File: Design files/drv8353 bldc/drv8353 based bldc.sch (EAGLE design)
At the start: 117 parts, among them IC1 DRV8353RSRGZT, J3 2X6 FEMALE, J4 B06B-HCMKK, Q1 FDBL86062-F085, Q2 FDBL86062-F085, Q3 FDBL86062-F085, Q4 FDBL86062-F085, Q5 FDBL86062-F085, Q6 FDBL86062-F085

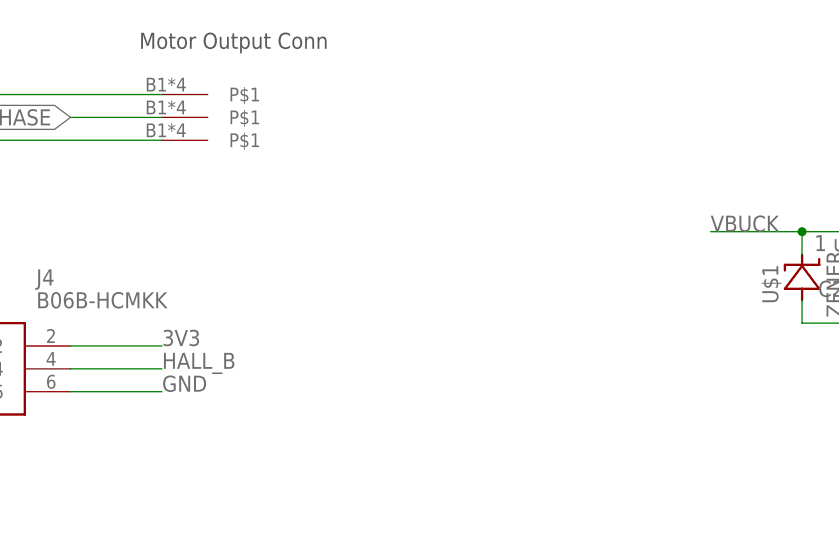
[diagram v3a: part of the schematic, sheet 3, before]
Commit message: adds correct circuitry for hall effect sensors
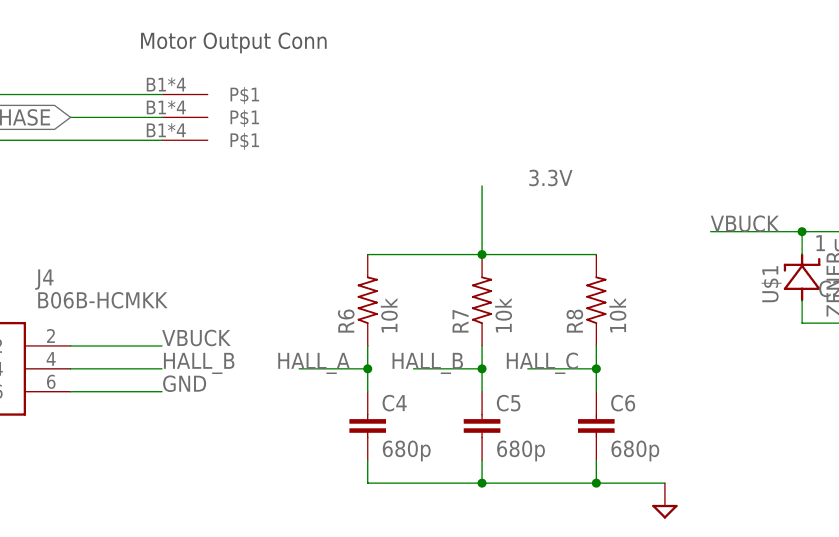
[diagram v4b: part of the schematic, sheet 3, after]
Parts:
- added C4, C5, C6: 680p, rcl:C-EUC0603K
- added R6, R7, R8: 10k, rcl:R-US_R0603
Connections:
- new net 3.3V: R6.2, R7.2, R8.2
- net 3V3: no longer J4.2
- net GND: now also C4.2, C5.2, C6.2
- net HALL_A: now also C4.1, R6.1
- net HALL_B: now also C5.1, R7.1
- net HALL_C: now also C6.1, R8.1
- net VBUCK: now also J4.2
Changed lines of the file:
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@@
 <part name="Q5" library="SamacSys_Parts" deviceset="FDBL86062-F085" device=""/>
 <part name="Q6" library="SamacSys_Parts" deviceset="FDBL86062-F085" device=""/>
+<part name="R6" library="rcl" library_urn="urn:adsk.eagle:library:334" deviceset="R-US_" device="R0603" package3d_urn="urn:adsk.eagle:package:23555/3" value="10k"/>
+<part name="R7" library="rcl" library_urn="urn:adsk.eagle:library:334" deviceset="R-US_" device="R0603" package3d_urn="urn:adsk.eagle:package:23555/3" value="10k"/>
+<part name="R8" library="rcl" library_urn="urn:adsk.eagle:library:334" deviceset="R-US_" device="R0603" package3d_urn="urn:adsk.eagle:package:23555/3" value="10k"/>
+<part name="C4" library="rcl" library_urn="urn:adsk.eagle:library:334" deviceset="C-EU" device="C0603K" package3d_urn="urn:adsk.eagle:package:23680/2" value="680p"/>
+<part name="C5" library="rcl" library_urn="urn:adsk.eagle:library:334" deviceset="C-EU" device="C0603K" package3d_urn="urn:adsk.eagle:package:23680/2" value="680p"/>
+<part name="C6" library="rcl" library_urn="urn:adsk.eagle:library:334" deviceset="C-EU" device="C0603K" package3d_urn="urn:adsk.eagle:package:23680/2" value="680p"/>
+<part name="SUPPLY12" library="supply2" library_urn="urn:adsk.eagle:library:372" deviceset="GND" device=""/>
 </parts>
 <sheets>
@@
 <attribute name="VALUE" x="201.93" y="-12.7" size="1.778" layer="96"/>
 </instance>
+<instance part="R6" gate="G$1" x="78.74" y="-10.16" smashed="yes" rot="R90">
+<attribute name="NAME" x="77.2414" y="-13.97" size="1.778" layer="95" rot="R90"/>
+<attribute name="VALUE" x="82.042" y="-13.97" size="1.778" layer="96" rot="R90"/>
+</instance>
+<instance part="R7" gate="G$1" x="91.44" y="-10.16" smashed="yes" rot="R90">
+<attribute name="NAME" x="89.9414" y="-13.97" size="1.778" layer="95" rot="R90"/>
+<attribute name="VALUE" x="94.742" y="-13.97" size="1.778" layer="96" rot="R90"/>
+</instance>
+<instance part="R8" gate="G$1" x="104.14" y="-10.16" smashed="yes" rot="R90">
+<attribute name="NAME" x="102.6414" y="-13.97" size="1.778" layer="95" rot="R90"/>
+<attribute name="VALUE" x="107.442" y="-13.97" size="1.778" layer="96" rot="R90"/>
+</instance>
+<instance part="C4" gate="G$1" x="78.74" y="-22.86" smashed="yes">
+<attribute name="NAME" x="80.264" y="-22.479" size="1.778" layer="95"/>
+<attribute name="VALUE" x="80.264" y="-27.559" size="1.778" layer="96"/>
+</instance>
+<instance part="C5" gate="G$1" x="91.44" y="-22.86" smashed="yes">
+<attribute name="NAME" x="92.964" y="-22.479" size="1.778" layer="95"/>
+<attribute name="VALUE" x="92.964" y="-27.559" size="1.778" layer="96"/>
+</instance>
+<instance part="C6" gate="G$1" x="104.14" y="-22.86" smashed="yes">
+<attribute name="NAME" x="105.664" y="-22.479" size="1.778" layer="95"/>
+<attribute name="VALUE" x="105.664" y="-27.559" size="1.778" layer="96"/>
+</instance>
+<instance part="SUPPLY12" gate="GND" x="111.76" y="-33.02" smashed="yes"/>
 </instances>
 <busses>
@@
 <label x="198.12" y="12.7" size="1.778" layer="95"/>
 </segment>
+<segment>
+<pinref part="C6" gate="G$1" pin="2"/>
+<wire x1="104.14" y1="-27.94" x2="104.14" y2="-30.48" width="0.1524" layer="91"/>
+<wire x1="104.14" y1="-30.48" x2="91.44" y2="-30.48" width="0.1524" layer="91"/>
+<pinref part="C5" gate="G$1" pin="2"/>
+<wire x1="91.44" y1="-30.48" x2="91.44" y2="-27.94" width="0.1524" layer="91"/>
+<pinref part="C4" gate="G$1" pin="2"/>
+<wire x1="78.74" y1="-27.94" x2="78.74" y2="-30.48" width="0.1524" layer="91"/>
+<wire x1="78.74" y1="-30.48" x2="91.44" y2="-30.48" width="0.1524" layer="91"/>
+<junction x="91.44" y="-30.48"/>
+<wire x1="104.14" y1="-30.48" x2="111.76" y2="-30.48" width="0.1524" layer="91"/>
+<junction x="104.14" y="-30.48"/>
+<pinref part="SUPPLY12" gate="GND" pin="GND"/>
+</segment>
 </net>
 <net name="VSENVM" class="0">
@@
 <junction x="127" y="-2.54"/>
 </segment>
-</net>
-<net name="3V3" class="0">
 <segment>
 <pinref part="J4" gate="G$1" pin="2"/>
@@
 <label x="55.88" y="-15.24" size="1.778" layer="95"/>
 </segment>
+</net>
+<net name="3V3" class="0">
 <segment>
 <pinref part="JP1" gate="G$1" pin="2"/>
@@
 <label x="55.88" y="-17.78" size="1.778" layer="95"/>
 </segment>
+<segment>
+<pinref part="R7" gate="G$1" pin="1"/>
+<pinref part="C5" gate="G$1" pin="1"/>
+<wire x1="91.44" y1="-15.24" x2="91.44" y2="-17.78" width="0.1524" layer="91"/>
+<wire x1="91.44" y1="-17.78" x2="91.44" y2="-20.32" width="0.1524" layer="91"/>
+<wire x1="91.44" y1="-17.78" x2="83.82" y2="-17.78" width="0.1524" layer="91"/>
+<junction x="91.44" y="-17.78"/>
+<label x="81.28" y="-17.78" size="1.778" layer="95"/>
+</segment>
 </net>
 <net name="HALL_A" class="0">
@@
 <label x="5.08" y="-17.78" size="1.778" layer="95"/>
 </segment>
+<segment>
+<pinref part="R6" gate="G$1" pin="1"/>
+<pinref part="C4" gate="G$1" pin="1"/>
+<wire x1="78.74" y1="-15.24" x2="78.74" y2="-17.78" width="0.1524" layer="91"/>
+<wire x1="78.74" y1="-17.78" x2="78.74" y2="-20.32" width="0.1524" layer="91"/>
+<wire x1="78.74" y1="-17.78" x2="71.12" y2="-17.78" width="0.1524" layer="91"/>
+<junction x="78.74" y="-17.78"/>
+<label x="68.58" y="-17.78" size="1.778" layer="95"/>
+</segment>
 </net>
 <net name="HALL_C" class="0">
@@
 <wire x1="25.4" y1="-20.32" x2="15.24" y2="-20.32" width="0.1524" layer="91"/>
 <label x="5.08" y="-20.32" size="1.778" layer="95"/>
+</segment>
+<segment>
+<pinref part="R8" gate="G$1" pin="1"/>
+<pinref part="C6" gate="G$1" pin="1"/>
+<wire x1="104.14" y1="-15.24" x2="104.14" y2="-17.78" width="0.1524" layer="91"/>
+<wire x1="104.14" y1="-17.78" x2="104.14" y2="-20.32" width="0.1524" layer="91"/>
+<wire x1="104.14" y1="-17.78" x2="96.52" y2="-17.78" width="0.1524" layer="91"/>
+<junction x="104.14" y="-17.78"/>
+<label x="93.98" y="-17.78" size="1.778" layer="95"/>
 </segment>
 </net>
@@
 </segment>
 </net>
+<net name="3.3V" class="0">
+<segment>
+<pinref part="R6" gate="G$1" pin="2"/>
+<pinref part="R7" gate="G$1" pin="2"/>
+<wire x1="78.74" y1="-5.08" x2="91.44" y2="-5.08" width="0.1524" layer="91"/>
+<pinref part="R8" gate="G$1" pin="2"/>
+<wire x1="104.14" y1="-5.08" x2="91.44" y2="-5.08" width="0.1524" layer="91"/>
+<junction x="91.44" y="-5.08"/>
+<wire x1="91.44" y1="-5.08" x2="91.44" y2="2.54" width="0.1524" layer="91"/>
+<label x="96.52" y="2.54" size="1.778" layer="95"/>
+</segment>
+</net>

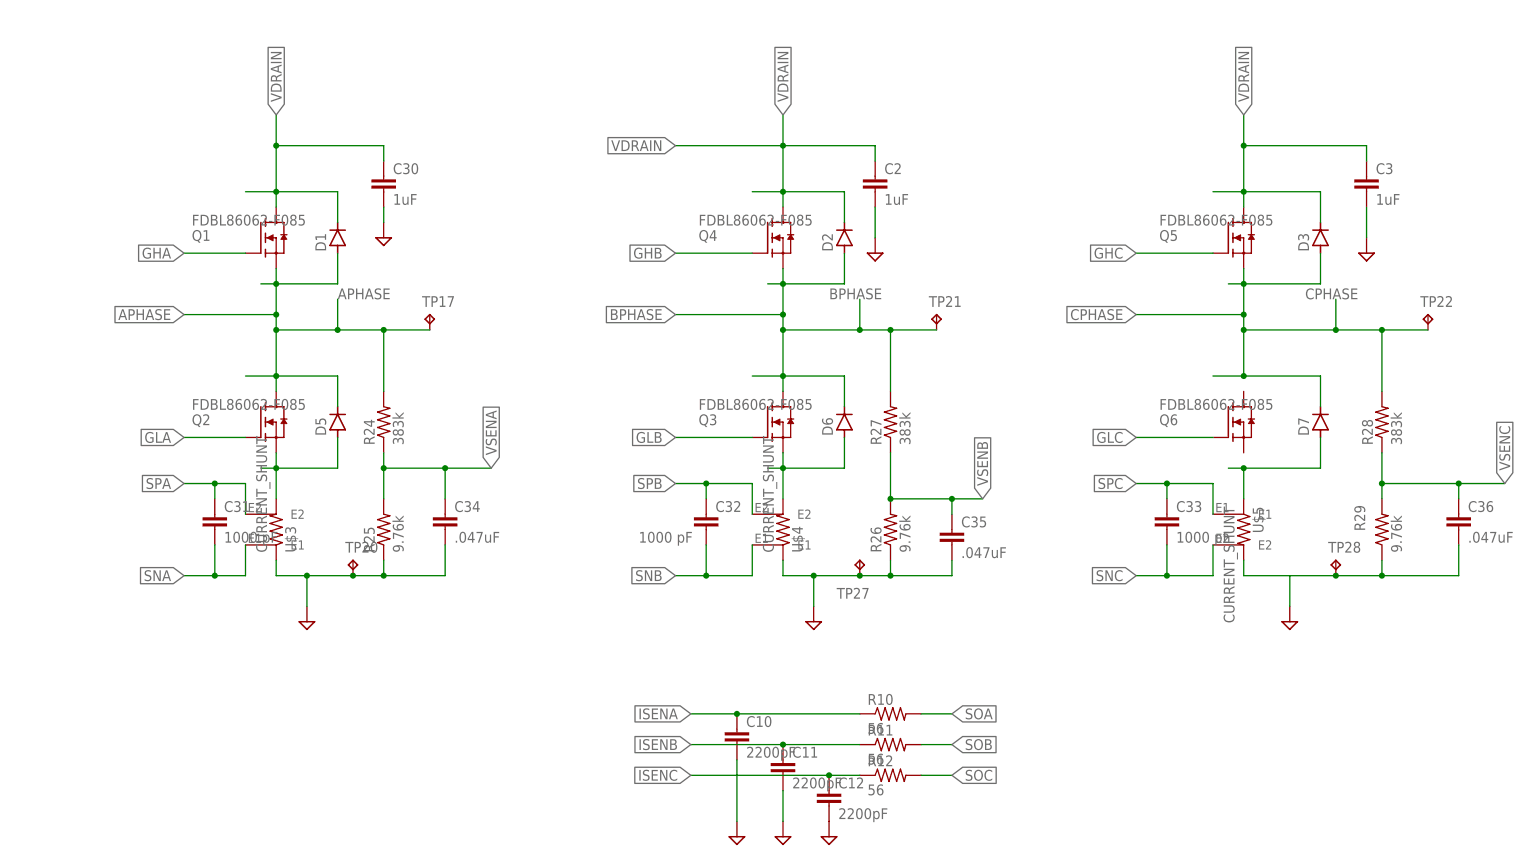
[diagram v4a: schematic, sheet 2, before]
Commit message: adds gate zeners protection
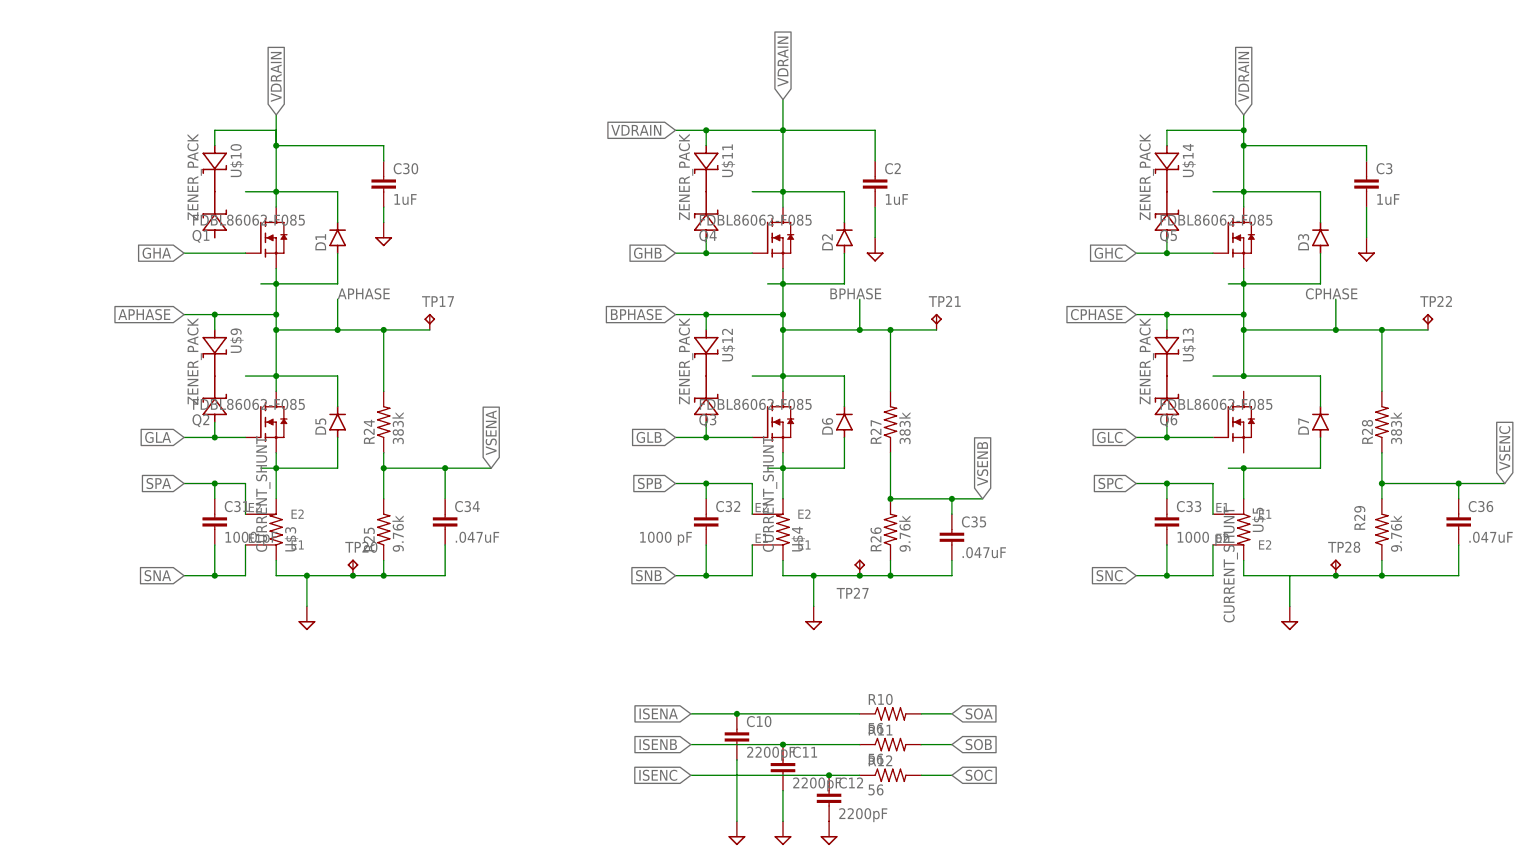
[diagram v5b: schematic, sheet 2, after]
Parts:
- added U$10, U$11, U$12, U$13, U$14, U$9: ZENER_PACK, SamacSys_Parts:ZENER_PACK
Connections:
- net APHASE: now also U$9.END2
- net BPHASE: now also U$12.END2
- net CPHASE: now also U$13.END2
- net GHB: now also U$11.END1
- net GHC: now also U$14.END1
- net GLA: now also U$9.END1
- net GLB: now also U$12.END1
- net GLC: now also U$13.END1
- net VDRAIN: now also U$10.END2, U$11.END2, U$14.END2

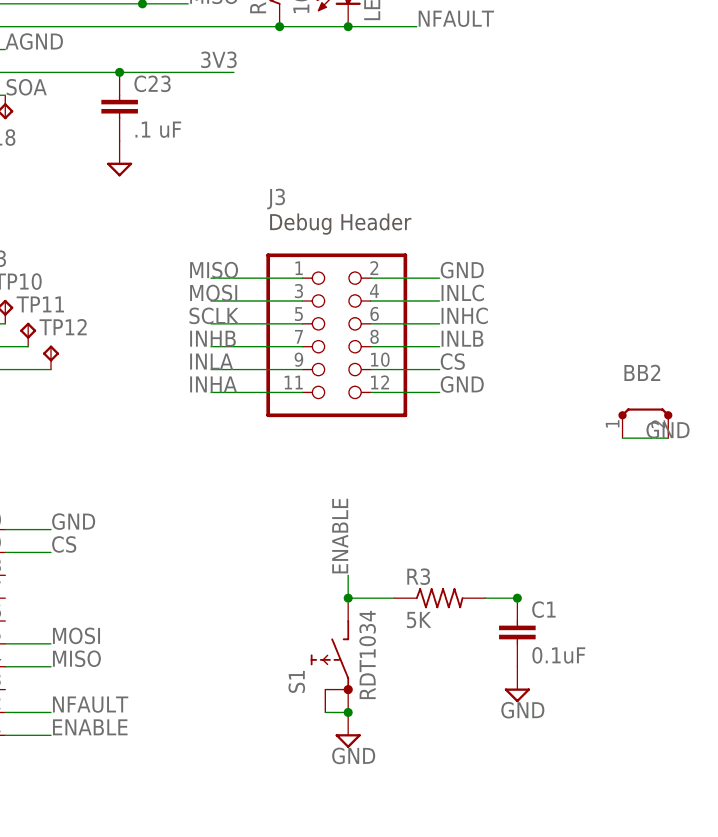
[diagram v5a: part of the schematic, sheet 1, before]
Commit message: expanded debug header
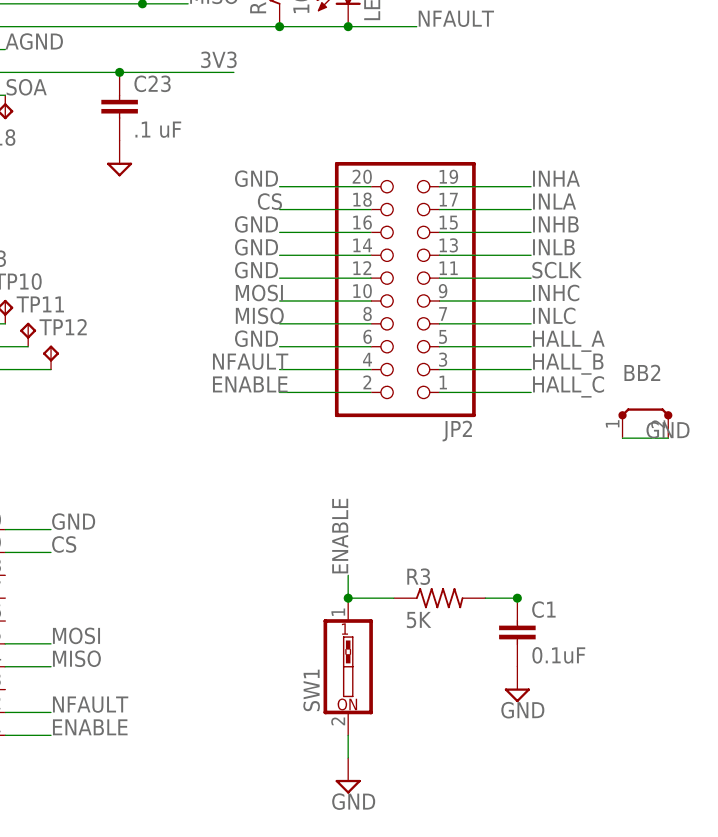
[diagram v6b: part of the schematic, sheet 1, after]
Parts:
- removed J3: 2X6 FEMALE, pinhead:PINHD-2X6
- removed S1: RDT1034, switch:RDT1034
- added JP2: (no value), pinhead:PINHD-2X10
- added SW1: (no value), special:SW_DIP-1
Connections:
- net CS: now also JP2.18; no longer J3.10
- net ENABLE: now also JP2.2, SW1.1; no longer S1.B
- net GND: now also JP2.12, JP2.14, JP2.16, JP2.20, JP2.6, SW1.2; no longer J3.12, J3.2, S1.A, S1.A1
- net HALL_A: now also JP2.5
- net HALL_B: now also JP2.3
- net HALL_C: now also JP2.1
- net INHA: now also JP2.19; no longer J3.11
- net INHB: now also JP2.15; no longer J3.7
- net INHC: now also JP2.9; no longer J3.6
- net INLA: now also JP2.17; no longer J3.9
- net INLB: now also JP2.13; no longer J3.8
- net INLC: now also JP2.7; no longer J3.4
- net MISO: now also JP2.8; no longer J3.1
- net MOSI: now also JP2.10; no longer J3.3
- net NFAULT: now also JP2.4
- net SCLK: now also JP2.11; no longer J3.5
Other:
- note removed: "Debug Header"

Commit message: initial commit
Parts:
- removed C23: .1 uF, resistor:C-EUC0603K
- removed C31, C32, C33: 1000 pF, rcl:C-EUC0603K
- removed IC1: DRV8353RSRGZT, REV BLDC:DRV8353RSRGZT
- removed R4: 0, resistor:R-US_R0603
- removed TP1, TP18, TP2, TP3, TP35, TP4, TP40: TPB1,27, testpad:TPB1,27
- added C7, C8, C9: (no value), resistor:C-EUC0603K
- added U$15: LM5008A_NGU_8, LM5008A:LM5008A_NGU_8
- added U1: Value, drv 8350 S:DRV8350SRTVR
- U$3, U$4, U$5: value CURRENT_SHUNT -> ACS78X; device REV BLDC:CURRENT_SHUNT -> REV BLDC:ACS78X
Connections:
- removed net AGND: IC1.AGND, R4.1, TP40.TP
- removed net CPH: C21.2, IC1.CPH
- removed net CPL: C21.1, IC1.CPL
- removed net N$22: D6.A, Q3.S, U$4.I2
- removed net N$24: D5.A, Q2.S, U$3.I2
- removed net N$27: D7.A, U$5.I1
- removed net SNA: C31.2, IC1.SNA, TP35.TP, U$3.E1
- removed net SNB: C32.2, IC1.SNB, TP4.TP, U$4.E1
- removed net SNC: C33.2, IC1.SNC, TP3.TP, U$5.E2
- removed net SPA: C31.1, IC1.SPA, TP34.TP, U$3.E2
- removed net SPB: C32.1, IC1.SPB, TP5.TP, U$4.E2
- removed net SPC: C33.1, IC1.SPC, TP10.TP, U$5.E1
- removed net VCP: C22.2, IC1.VCP
- removed net VGLS: C16.2, IC1.VGLS
- new net N$3: C22.2, U1.VCP
- new net N$4: C21.2, U1.CPH
- new net N$5: C21.1, U1.CPL
- new net N$6: C16.2, U1.VGLS
- new net N$8: C8.2, U$4.GND, U$4.NC1, U$4.NC2
- new net SLA: D5.A, Q2.S, TP34.TP, U$3.IP+, U1.SLA
- new net SLB: D6.A, Q3.S, TP5.TP, U$4.IP+, U1.SLB
- new net SLC: D7.A, TP10.TP, U$5.IP+, U1.SLC
- net 3V3: now also C7.2, C8.1, C9.1, U$3.VCC, U$4.VCC, U$5.VCC; no longer C23.1, IC1.VREF
- net APHASE: now also U1.SHA; no longer IC1.SHA
- net BPHASE: now also U1.SHB; no longer IC1.SHB
- net BST: now also U$15.BST; no longer IC1.BST
- net CPHASE: now also U1.SHC; no longer IC1.SHC
- net CS: now also U1.SCS_N; no longer IC1.NSCS
- net DRV_VM: now also U1.VM; no longer IC1.VM
- net ENABLE: now also U1.ENABLE; no longer IC1.ENABLE
- net FB: now also U$15.FB; no longer IC1.FB
- net GHA: now also U1.GHA; no longer IC1.GHA
- net GHB: now also U1.GHB; no longer IC1.GHB
- net GHC: now also U1.GHC; no longer IC1.GHC
- net GLA: now also U1.GLA; no longer IC1.GLA
- net GLB: now also U1.GLB; no longer IC1.GLB
- net GLC: now also U1.GLC; no longer IC1.GLC
- net GND: now also C7.1, C9.2, U$15.EP, U$15.RTN, U$3.GND, U$3.IP-, U$3.NC1, U$3.NC2, U$4.IP-, U$5.GND, U$5.IP-, U$5.NC1, U$5.NC2, U1.PAD, U1.PGND; no longer C23.2, IC1.DGND, IC1.GND_1, IC1.GND_2, R4.2, U$3.I1, U$4.I1, U$5.I2
- net INHA: now also U1.INHA; no longer IC1.INHA
- net INHB: now also U1.INHB; no longer IC1.INHB
- net INHC: now also U1.INHC; no longer IC1.INHC
- net INLA: now also U1.INLA; no longer IC1.INLA
- net INLB: now also U1.INLB; no longer IC1.INLB
- net INLC: now also U1.INLC; no longer IC1.INLC
- net MISO: now also U1.SDO; no longer IC1.SDO
- net MOSI: now also U1.SDI; no longer IC1.SDI
- net N$1: now also U1.DVDD; no longer IC1.DVDD
- net NFAULT: now also U1.FAULT_N; no longer IC1.NFAULT
- net RCL: now also U$15.RCL; no longer IC1.RCL
- net RT/SD: now also U$15.RT/SD; no longer IC1.RT/SD
- net SCLK: now also U1.SCLK; no longer IC1.SCLK
- net SOA: now also U$3.VOUT; no longer IC1.SOA, TP18.TP
- net SOB: now also U$4.VOUT; no longer IC1.SOB, TP1.TP
- net SOC: now also U$5.VOUT; no longer IC1.SOC, TP2.TP
- net SW: now also U$15.SW; no longer IC1.SW
- net VCC: now also U$15.VCC; no longer IC1.VCC
- net VDRAIN: now also U$15.VIN, U1.VDRAIN; no longer IC1.VDRAIN, IC1.VIN
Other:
- moved on the sheet: BB2, C1, C13, C14, C15, C16, C17, C18, C19, C20, C22, C25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
